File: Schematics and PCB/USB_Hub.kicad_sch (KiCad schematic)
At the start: 98 parts, among them J10 Conn_01x12, J6 UPSTREAM, J7 DOWNSTREAM_3, J8 DOWNSTREAM_1, J9 DOWNSTREAM_2, U16 TUSB8042A, U17 TPS2561, U18 TLV71311PDBVR, U19 TLV70033DDCR, U20 TPS2561, Y1 24MHz 20pF GND24

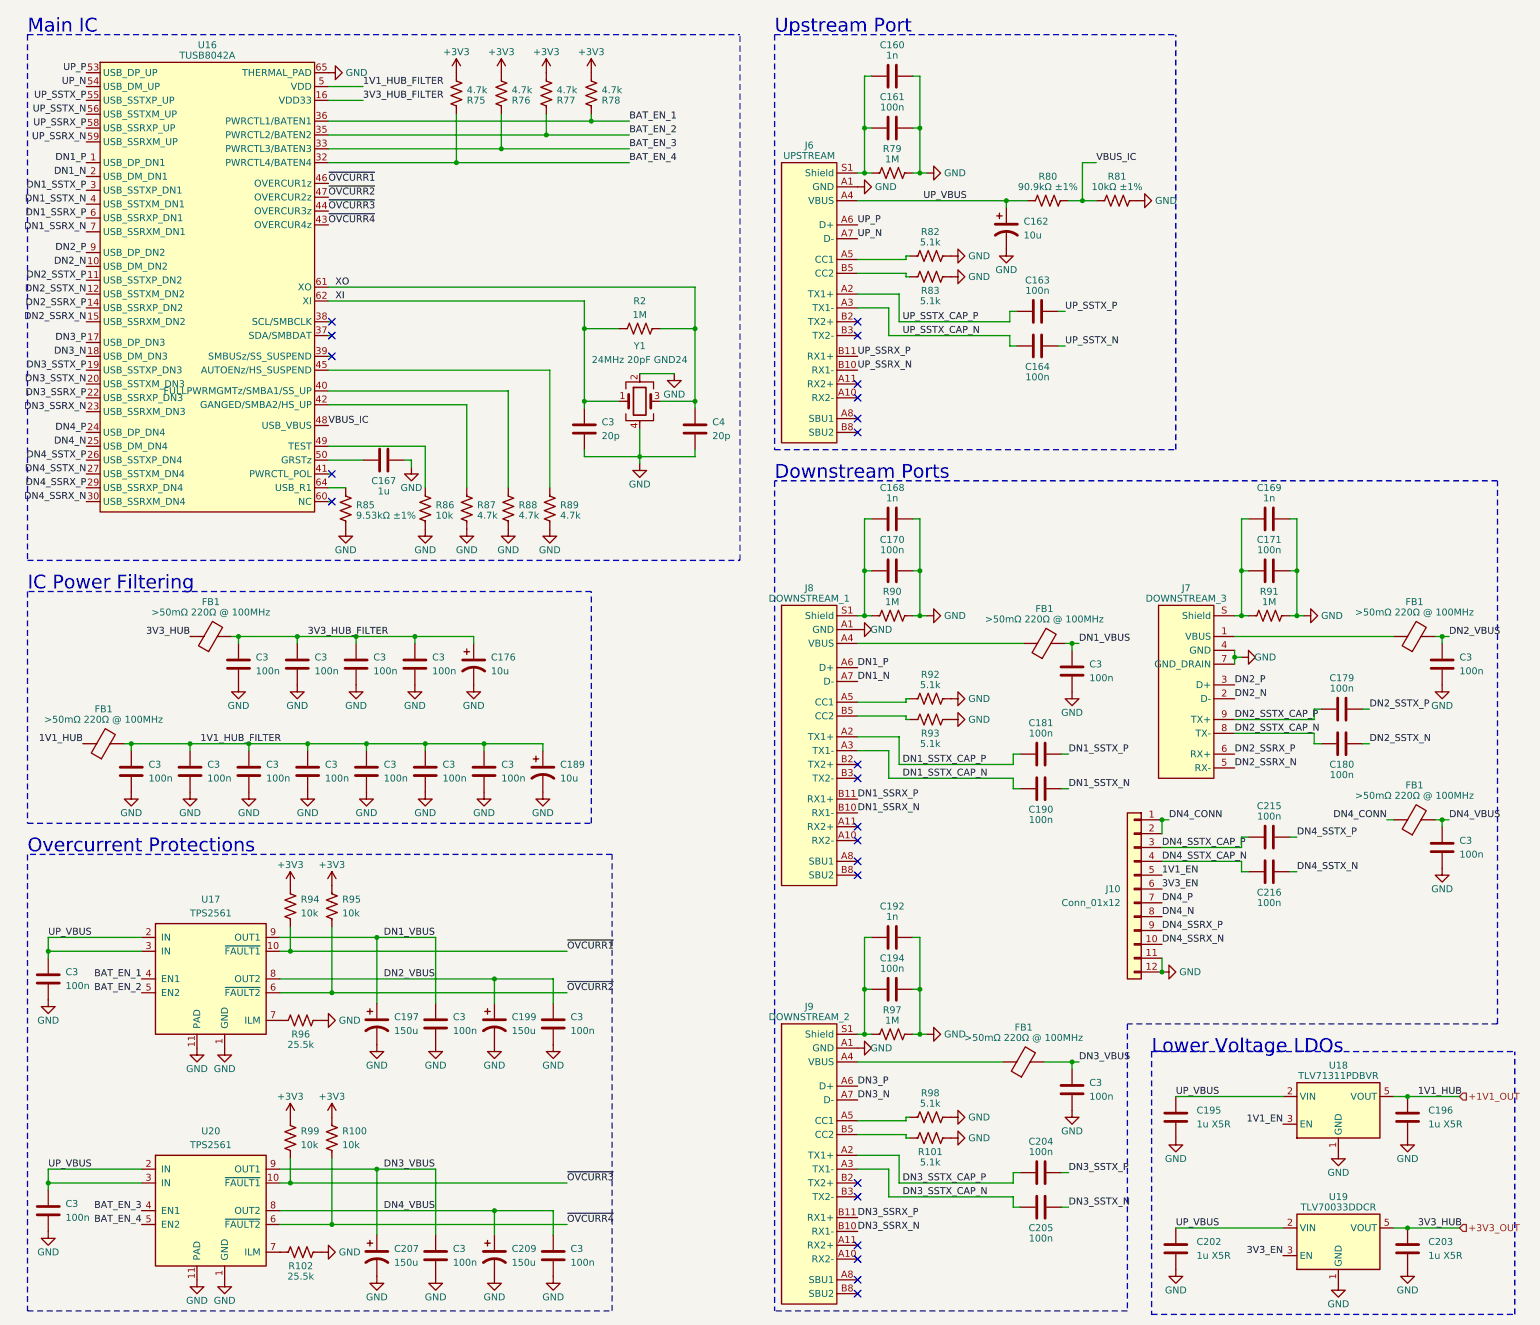
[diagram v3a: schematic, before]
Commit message: More Hub routing
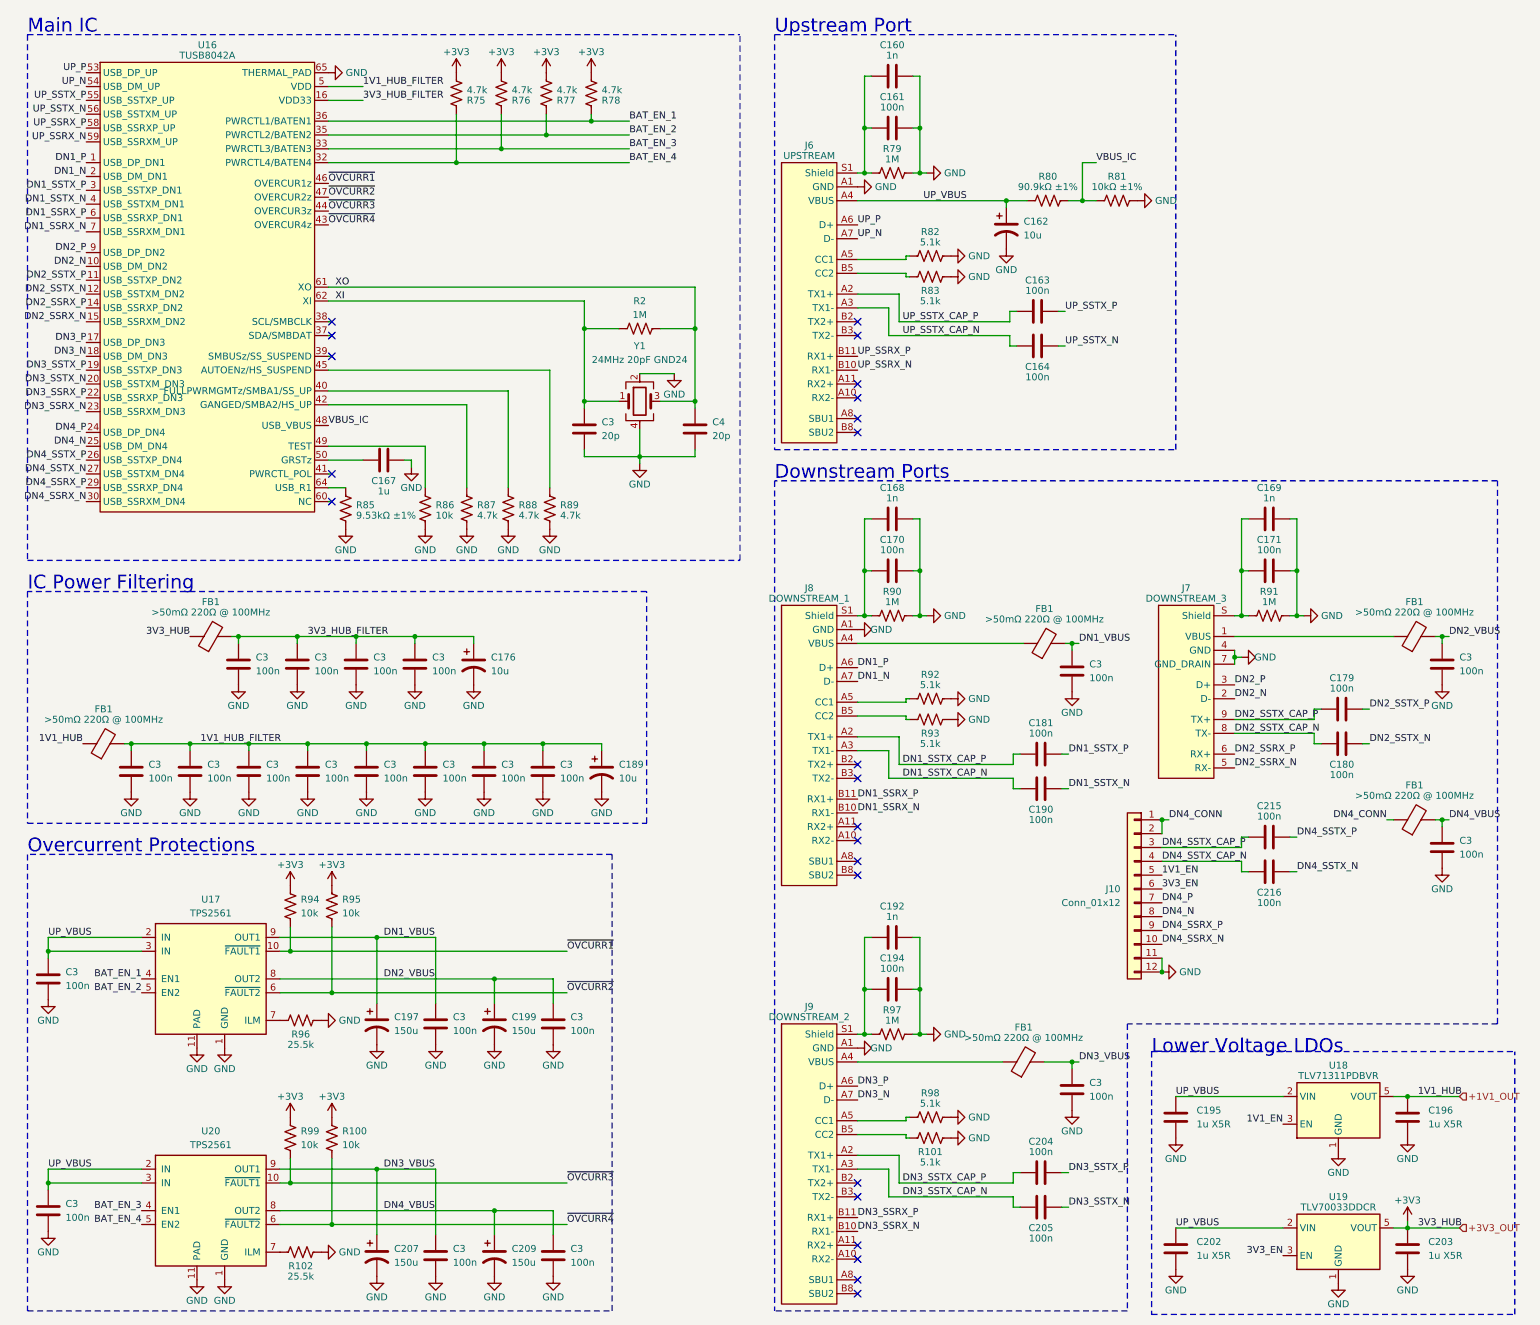
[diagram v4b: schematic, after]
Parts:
- added C3: 100n, Capacitor_SMD:C_0603_1608Metric, symbol Device:C
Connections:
- net +3V3_OUT is gone; now on net +3V3: C203.1, FB1.1, U19.5 (VOUT)
- net 1V1_HUB_FILTER: now also C3.1
- net GND: now also C3.2
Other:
- moved on the sheet: C189
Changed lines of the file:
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@@
   (junction (at 170.815 192.405) (diameter 0) (color 0 0 0 0)
   )
+  (junction (at 111.76 147.32) (diameter 0) (color 0 0 0 0)
+  )
   (junction (at 129.54 94.615) (diameter 0) (color 0 0 0 0)
   )
@@
     (stroke (width 0) (type default))
   )
+  (wire (pts (xy 111.76 147.32) (xy 111.76 148.59))
+    (stroke (width 0) (type default))
+  )
   (polyline (pts (xy 154.305 93.345) (xy 227.965 93.345))
     (stroke (width 0) (type dash))
@@
     (stroke (width 0) (type default))
   )
+  (wire (pts (xy 270.51 234.95) (xy 270.51 236.22))
+    (stroke (width 0) (type default))
+  )
   (wire (pts (xy 139.7 94.615) (xy 139.7 93.345))
     (stroke (width 0) (type default))
@@
     (stroke (width 0) (type default))
   )
-  (polyline (pts (xy 17.145 161.925) (xy 120.65 161.925))
+  (polyline (pts (xy 17.145 161.925) (xy 130.81 161.925))
     (stroke (width 0) (type dash))
   )
@@
     (stroke (width 0) (type default))
   )
-  (polyline (pts (xy 120.65 119.38) (xy 17.145 119.38))
+  (polyline (pts (xy 130.81 119.38) (xy 17.145 119.38))
     (stroke (width 0) (type dash))
   )
@@
     (stroke (width 0) (type default))
   )
+  (wire (pts (xy 111.76 147.32) (xy 122.555 147.32))
+    (stroke (width 0) (type default))
+  )
   (wire (pts (xy 169.545 219.075) (xy 178.435 219.075))
     (stroke (width 0) (type default))
@@
     (stroke (width 0) (type default))
   )
-  (wire (pts (xy 111.76 147.32) (xy 111.76 148.59))
+  (wire (pts (xy 122.555 147.32) (xy 122.555 148.59))
     (stroke (width 0) (type default))
   )
@@
     (stroke (width 0) (type default))
   )
-  (polyline (pts (xy 120.65 161.925) (xy 120.65 119.38))
+  (polyline (pts (xy 130.81 161.925) (xy 130.81 119.38))
     (stroke (width 0) (type dash))
   )
@@
     )
   )
+  (symbol (lib_id "power:+3V3") (at 270.51 234.95 0) (mirror y) (unit 1)
+    (in_bom yes) (on_board yes) (dnp no)
+    (property "Reference" "#PWR0552" (at 270.51 238.76 0)
+      (effects (font (size 1.27 1.27)) hide)
+    )
+    (property "Value" "+3V3" (at 270.51 231.14 0)
+      (effects (font (size 1.27 1.27)))
+    )
+    (property "Footprint" "" (at 270.51 234.95 0)
+      (effects (font (size 1.27 1.27)) hide)
+    )
+    (property "Datasheet" "" (at 270.51 234.95 0)
+      (effects (font (size 1.27 1.27)) hide)
+    )
+    (pin "1")
+    (instances
+      (project "Schematics and PCB"
+        (path "/e4b186e2-256b-418b-b9a4-327a6681c2f1/8c37ee3d-25d1-4c2c-ab3c-fab92c9b18c9"
+          (reference "#PWR0552") (unit 1)
+        )
+      )
+    )
+  )
   (symbol (lib_id "Regulator_Linear:ADP7182AUJZ-1.8") (at 257.81 238.76 0) (mirror x) (unit 1)
     (in_bom yes) (on_board yes) (dnp no)
@@
     )
   )
+  (symbol (lib_id "Device:C") (at 111.76 152.4 0) (unit 1)
+    (in_bom yes) (on_board yes) (dnp no)
+    (property "Reference" "C3" (at 114.935 151.13 0)
+      (effects (font (size 1.27 1.27)) (justify left))
+    )
+    (property "Value" "100n" (at 114.935 153.67 0)
+      (effects (font (size 1.27 1.27)) (justify left))
+    )
+    (property "Footprint" "Capacitor_SMD:C_0603_1608Metric" (at 112.7252 156.21 0)
+      (effects (font (size 1.27 1.27)) hide)
+    )
+    (property "Datasheet" "~" (at 111.76 152.4 0)
+      (effects (font (size 1.27 1.27)) hide)
+    )
+    (pin "1")
+    (pin "2")
+    (instances
+      (project "Schematics and PCB"
+        (path "/e4b186e2-256b-418b-b9a4-327a6681c2f1"
+          (reference "C3") (unit 1)
+        )
+        (path "/e4b186e2-256b-418b-b9a4-327a6681c2f1/830e000a-0352-489c-8287-8192b33ea35f"
+          (reference "C3") (unit 1)
+        )
+        (path "/e4b186e2-256b-418b-b9a4-327a6681c2f1/8a6a2f38-9d1f-4150-b845-3f93155a132a"
+          (reference "C126") (unit 1)
+        )
+        (path "/e4b186e2-256b-418b-b9a4-327a6681c2f1/83096c47-2ee4-4d73-99aa-4d3823825a69"
+          (reference "C141") (unit 1)
+        )
+        (path "/e4b186e2-256b-418b-b9a4-327a6681c2f1/8c37ee3d-25d1-4c2c-ab3c-fab92c9b18c9"
+          (reference "C217") (unit 1)
+        )
+      )
+    )
+  )
   (symbol (lib_id "power:GND") (at 48.26 203.2 0) (unit 1)
     (in_bom yes) (on_board yes) (dnp no)
@@
     )
   )
-  (symbol (lib_id "Device:C_Polarized_US") (at 111.76 152.4 0) (unit 1)
+  (symbol (lib_id "Device:C_Polarized_US") (at 122.555 152.4 0) (unit 1)
     (in_bom yes) (on_board yes) (dnp no)
-    (property "Reference" "C189" (at 114.935 151.13 0)
+    (property "Reference" "C189" (at 125.73 151.13 0)
       (effects (font (size 1.27 1.27)) (justify left))
     )
-    (property "Value" "10u" (at 114.935 153.67 0)
+    (property "Value" "10u" (at 125.73 153.67 0)
       (effects (font (size 1.27 1.27)) (justify left))
     )
-    (property "Footprint" "Capacitor_Tantalum_SMD:CP_EIA-3216-18_Kemet-A" (at 111.76 152.4 0)
+    (property "Footprint" "Capacitor_Tantalum_SMD:CP_EIA-3216-18_Kemet-A" (at 122.555 152.4 0)
       (effects (font (size 1.27 1.27)) hide)
     )
-    (property "Datasheet" "~" (at 111.76 152.4 0)
+    (property "Datasheet" "~" (at 122.555 152.4 0)
       (effects (font (size 1.27 1.27)) hide)
     )
@@
     )
   )
-  (symbol (lib_id "power:GND") (at 111.76 156.21 0) (unit 1)
+  (symbol (lib_id "power:GND") (at 122.555 156.21 0) (unit 1)
     (in_bom yes) (on_board yes) (dnp no)
-    (property "Reference" "#PWR07" (at 111.76 162.56 0)
+    (property "Reference" "#PWR07" (at 122.555 162.56 0)
       (effects (font (size 1.27 1.27)) hide)
     )
-    (property "Value" "GND" (at 111.76 160.02 0)
+    (property "Value" "GND" (at 122.555 160.02 0)
       (effects (font (size 1.27 1.27)))
     )
-    (property "Footprint" "" (at 111.76 156.21 0)
+    (property "Footprint" "" (at 122.555 156.21 0)
       (effects (font (size 1.27 1.27)) hide)
     )
-    (property "Datasheet" "" (at 111.76 156.21 0)
+    (property "Datasheet" "" (at 122.555 156.21 0)
       (effects (font (size 1.27 1.27)) hide)
     )
@@
         )
       )
+    )
+  )
+  (symbol (lib_id "power:GND") (at 111.76 156.21 0) (unit 1)
+    (in_bom yes) (on_board yes) (dnp no)
+    (property "Reference" "#PWR07" (at 111.76 162.56 0)
+      (effects (font (size 1.27 1.27)) hide)
+    )
+    (property "Value" "GND" (at 111.76 160.02 0)
+      (effects (font (size 1.27 1.27)))
+    )
+    (property "Footprint" "" (at 111.76 156.21 0)
+      (effects (font (size 1.27 1.27)) hide)
+    )
+    (property "Datasheet" "" (at 111.76 156.21 0)
+      (effects (font (size 1.27 1.27)) hide)
+    )
+    (pin "1")
+    (instances
+      (project "Schematics and PCB"
+        (path "/e4b186e2-256b-418b-b9a4-327a6681c2f1"
+          (reference "#PWR07") (unit 1)
+        )
+        (path "/e4b186e2-256b-418b-b9a4-327a6681c2f1/830e000a-0352-489c-8287-8192b33ea35f"
+          (reference "#PWR07") (unit 1)
+        )
+        (path "/e4b186e2-256b-418b-b9a4-327a6681c2f1/8a6a2f38-9d1f-4150-b845-3f93155a132a"
+          (reference "#PWR0281") (unit 1)
+        )
+        (path "/e4b186e2-256b-418b-b9a4-327a6681c2f1/83096c47-2ee4-4d73-99aa-4d3823825a69"
+          (reference "#PWR0316") (unit 1)
+        )
+        (path "/e4b186e2-256b-418b-b9a4-327a6681c2f1/8c37ee3d-25d1-4c2c-ab3c-fab92c9b18c9"
+          (reference "#PWR0551") (unit 1)
+        )
+      )
